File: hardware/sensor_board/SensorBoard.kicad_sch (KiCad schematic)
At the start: 76 parts, among them J1 Relay Board Connector, J10 GND BUS, J11 FEED SENSOR R1, J12 Relay Pull, J13 SPARE GPIO, J15 LED L1, J16 LED L2, J17 LED L3, J18 LED L4, J19 LED R1, J2 Pi 5V, J20 EXT, J21 LED R2, J22 LED R3, J23 LED R4, J24 Raspberry Pi GPIO header, J25 RTC Header, J26 I2C0, J27 I2C1, J28 I2C2, J29 I2C3, J3 Display 5V, J30 I2C4, J31 I2C5, J32 I2C6, J33 I2C7, J4 DC IN 5V, J5 VSYS BUS, J6 FEED SENSOR L2, J7 3V3 BUS, J8 FEED SENSOR R2, J9 FEED SENSOR L1, Q1 PN2222A, Q2 PN2222A, Q3 PN2222A, Q4 PN2222A, Q5 PN2222A, Q6 PN2222A, Q7 PN2222A, Q8 PN2222A, SW1 Pico Reset, U1 Raspberry Pico, U2 74HC595, U3 TCA9548A, U4 LM1117, U5 DS3231MZ, U6 74HC165

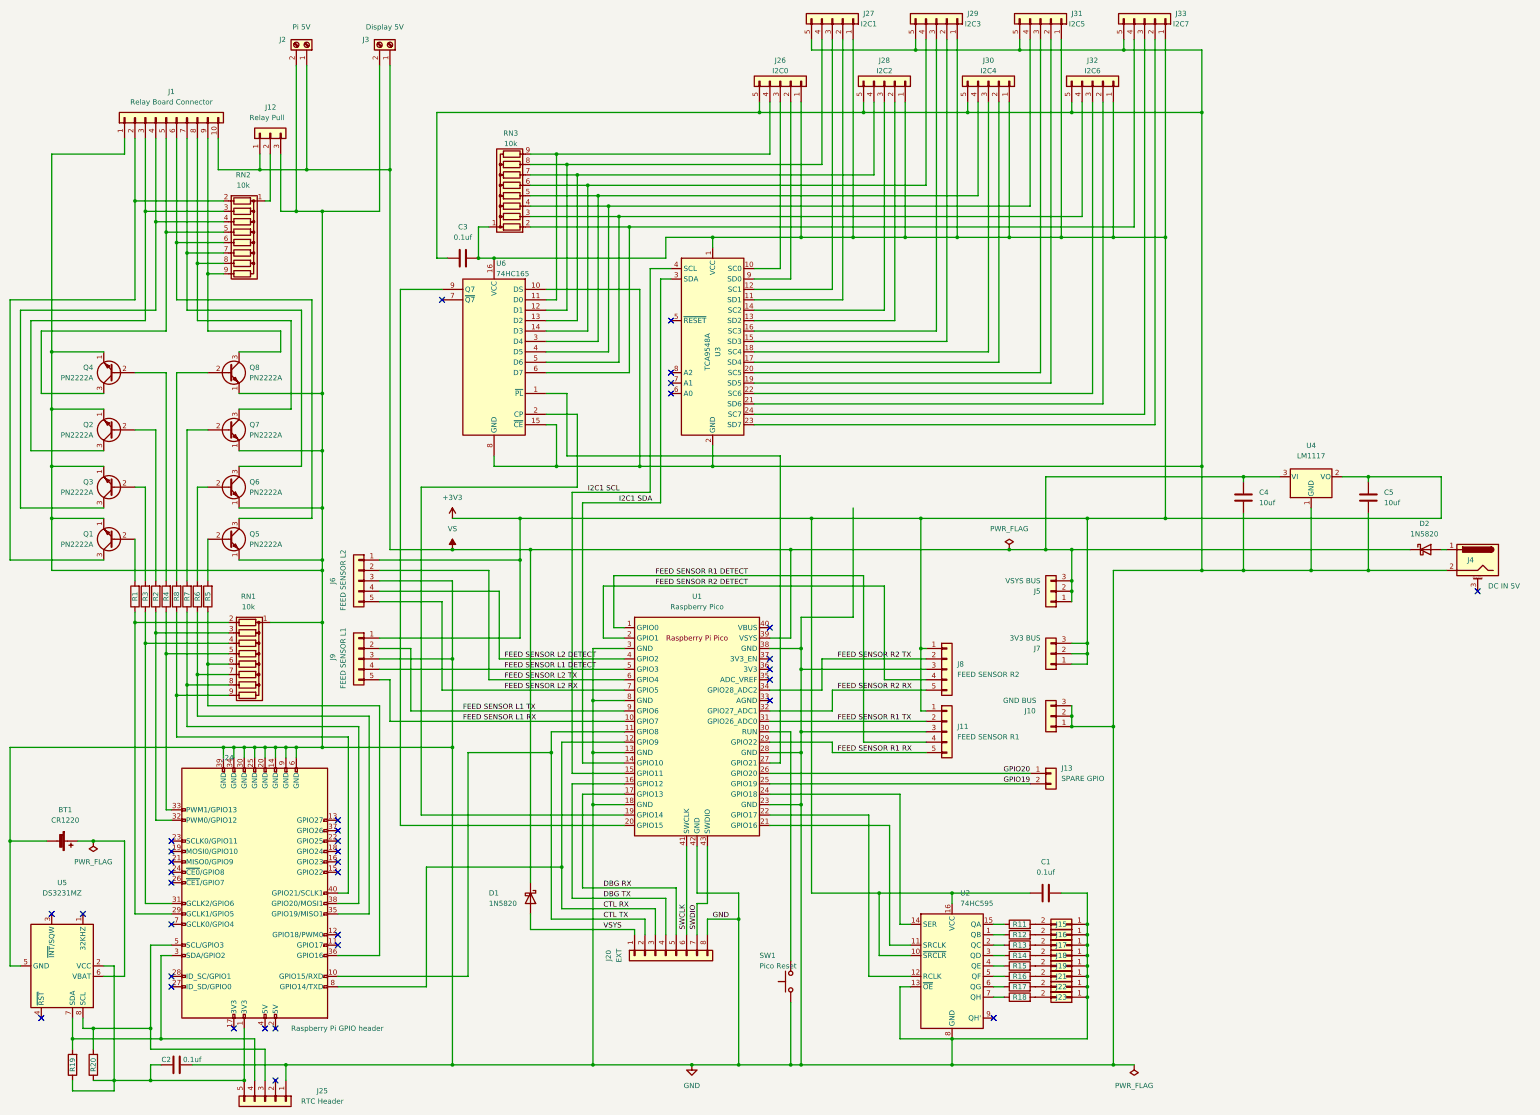
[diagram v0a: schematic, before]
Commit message: Trying out the idea of a hardware hat for the Pi rather than a whole separate board. Doesn't fit in my enclosure, though
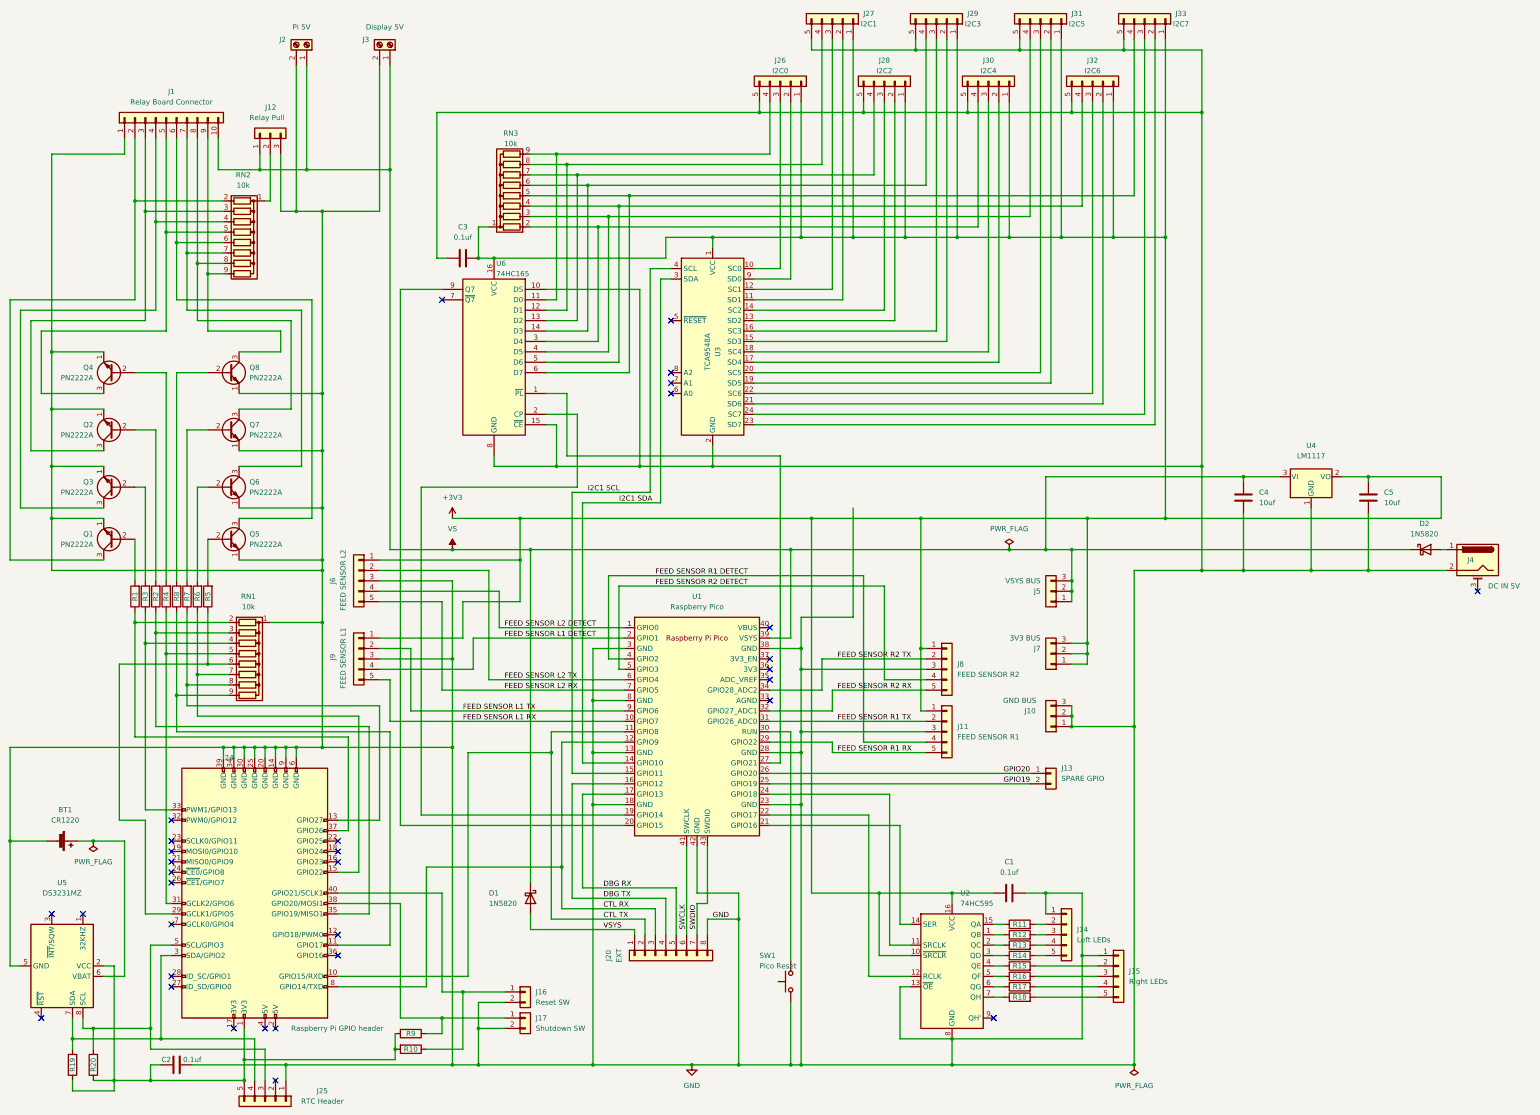
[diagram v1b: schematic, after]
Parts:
- removed J15: LED L1, Connector_JST:JST_XH_B2B-XH-A_1x02_P2.50mm_Vertical, symbol Connector_Generic:Conn_02x01
- removed J16: LED L2, Connector_JST:JST_XH_B2B-XH-A_1x02_P2.50mm_Vertical, symbol Connector_Generic:Conn_02x01
- removed J17: LED L3, Connector_JST:JST_XH_B2B-XH-A_1x02_P2.50mm_Vertical, symbol Connector_Generic:Conn_02x01
- removed J18: LED L4, Connector_JST:JST_XH_B2B-XH-A_1x02_P2.50mm_Vertical, symbol Connector_Generic:Conn_02x01
- removed J19: LED R1, Connector_JST:JST_XH_B2B-XH-A_1x02_P2.50mm_Vertical, symbol Connector_Generic:Conn_02x01
- removed J21: LED R2, Connector_JST:JST_XH_B2B-XH-A_1x02_P2.50mm_Vertical, symbol Connector_Generic:Conn_02x01
- removed J22: LED R3, Connector_JST:JST_XH_B2B-XH-A_1x02_P2.50mm_Vertical, symbol Connector_Generic:Conn_02x01
- removed J23: LED R4, Connector_JST:JST_XH_B2B-XH-A_1x02_P2.50mm_Vertical, symbol Connector_Generic:Conn_02x01
- added J14: Left LEDs, Connector_JST:JST_XH_B5B-XH-A_1x05_P2.50mm_Vertical, symbol Connector_Generic:Conn_01x05
- added J15: Right LEDs, Connector_JST:JST_XH_B5B-XH-A_1x05_P2.50mm_Vertical, symbol Connector_Generic:Conn_01x05
- added J16: Reset SW, Connector_JST:JST_XH_B2B-XH-A_1x02_P2.50mm_Vertical, symbol Connector_Generic:Conn_01x02
- added J17: Shutdown SW, Connector_JST:JST_XH_B2B-XH-A_1x02_P2.50mm_Vertical, symbol Connector_Generic:Conn_01x02
- added R10, R9: 10k, Resistor_THT:R_Axial_DIN0207_L6.3mm_D2.5mm_P7.62mm_Horizontal, symbol Device:R
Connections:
- net FEED SENSOR L1 DETECT: now also U1.2 (GPIO1); no longer U1.5 (GPIO3)
- net FEED SENSOR L2 DETECT: now also U1.1 (GPIO0); no longer U1.4 (GPIO2)
- net FEED SENSOR R1 DETECT: now also U1.4 (GPIO2); no longer U1.1 (GPIO0)
- net FEED SENSOR R2 DETECT: now also U1.5 (GPIO3); no longer U1.2 (GPIO1)
- net GND: now also J14.1 (Pin_1), J15.1 (Pin_1), J16.2 (Pin_2), J17.2 (Pin_2)
- net at R11.2: now also J14.2 (Pin_2)
- net at U2.11 (SRCLK): now also U1.24 (GPIO18); no longer U1.21 (GPIO16)
- net at U2.14 (SER): now also U1.21 (GPIO16); no longer U1.24 (GPIO18)
- net at J33.4 (Pin_4), U6.6 (D7): now also RN3.5 (R4); no longer RN3.2 (R1)
- net at R12.2: now also J14.3 (Pin_3)
- net at R8.1, RN1.9 (R8): now also J24.11 (GPIO17); no longer J24.40 (GPIO21/SCLK1)
- net at R18.2: now also J15.5 (Pin_5)
- net at J30.4 (Pin_4), U6.3 (D4): now also RN3.2 (R1); no longer RN3.5 (R4)
- net at J31.4 (Pin_4), U6.4 (D5): now also RN3.3 (R2); no longer RN3.4 (R3)
- net at J32.4 (Pin_4), U6.5 (D6): now also RN3.4 (R3); no longer RN3.3 (R2)
- net at R2.1, RN1.3 (R2): now also J24.35 (GPIO19/MISO1); no longer J24.32 (PWM0/GPIO12)
- net at R13.2: now also J14.4 (Pin_4)
- net at R17.2: now also J15.4 (Pin_4)
- net at C2.1, J24.1 (3V3), J25.5 (Pin_5)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: now also R10.2, R9.2
- net at R14.2: now also J14.5 (Pin_5)
- net at J24.13 (GPIO27): now also R7.1, RN1.8 (R7)
- net at J24.15 (GPIO22): now also R6.1, RN1.7 (R6)
- net at R1.1, RN1.2 (R1): now also J24.37 (GPIO26); no longer J24.29 (GCLK1/GPIO5)
- net at R3.1, RN1.4 (R3): now also J24.33 (PWM1/GPIO13); no longer J24.31 (GCLK2/GPIO6)
- net at R4.1, RN1.5 (R4): now also J24.31 (GCLK2/GPIO6); no longer J24.33 (PWM1/GPIO13)
- net at R5.1, RN1.6 (R5): now also J24.29 (GCLK1/GPIO5); no longer J24.36 (GPIO16)
- net at R15.2: now also J15.2 (Pin_2)
- net at R16.2: now also J15.3 (Pin_3)
- new net: J17.1 (Pin_1), J24.38 (GPIO20/MOSI1), R9.1
- new net: J16.1 (Pin_1), J24.40 (GPIO21/SCLK1), R10.1
- no-connect marks 35 -> 33
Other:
- moved on the sheet: C1
